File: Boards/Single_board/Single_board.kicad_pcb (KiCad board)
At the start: 2 copper layers, 170.1 x 185.4 mm, 116 parts, among them J1 Conn_01x04_Socket, J2 Conn_01x04_Socket, Q1 SI2306, Q10 SI2306, Q11 SI2306, Q12 SI2306, Q13 SI2306, Q14 SI2306, Q15 SI2306, Q2 SI2306, Q3 SI2306, Q4 SI2306, Q5 SI2306, Q6 SI2306, Q7 SI2306, Q8 SI2306, Q9 SI2306, SW1 +, SW10 5, SW11 2, SW12 9, SW13 PRO, SW14 6, SW15 3, SW16 CLR, SW17 ENTR, SW18 RSET, SW19 KEYREL, SW2 VERB, SW3 NOUN, SW4 0, SW5 7, SW6 -, SW7 4, SW8 1, SW9 8, U1 PCF8575

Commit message: some progress on the arduino boilerplate
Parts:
- removed A1: Arduino_Nano_Socket, PCM_arduino-library:Arduino_Nano_Socket
- added C3: 100nF, Capacitor_SMD:C_0805_2012Metric, F.Cu at (141.6, 146.4)
- added C4: 4.7uF, Capacitor_SMD:C_0805_2012Metric, F.Cu at (141.6, 152.2)
- added C5: 100nF, Capacitor_SMD:C_0805_2012Metric, F.Cu at (158.0, 151.2)
- added J3: USB_C_Receptacle_USB2.0_16P, Connector_USB:USB_C_Receptacle_G-Switch_GT-USB-7010ASV, F.Cu at (189.7, 149.3)
- added U2: ATmega328P-A, Package_QFP:TQFP-32_7x7mm_P0.8mm, F.Cu at (150.4, 149.8)
- added U3: CH340G, Package_SO:SOIC-16_3.9x9.9mm_P1.27mm, F.Cu at (172.0, 149.0)
- C1, C2: footprint Capacitor_SMD:C_1206_3216Metric_Pad1.33x1.80mm_HandSolder -> Capacitor_SMD:C_0805_2012Metric
- D20, D21, D22, D23, D24, D25, D26, D27, D28, D29, D30, D31, D32, D33: footprint LED_SMD:LED_1206_3216Metric_Pad1.42x1.75mm_HandSolder -> LED_SMD:LED_1206_3216Metric
- Q1, Q10, Q11, Q12, Q13, Q14, Q15, Q2, Q3, Q4, Q5, Q6, Q7, Q8, Q9: footprint Package_TO_SOT_SMD:SOT-23-3 -> Package_TO_SOT_SMD:SOT-23
- R1, R2, R3: footprint Resistor_SMD:R_1206_3216Metric_Pad1.30x1.75mm_HandSolder -> Resistor_SMD:R_1206_3216Metric
- R10, R11, R12, R13, R14, R15, R16, R17, R18, R19, R20, R21, R22, R23, R24, R25, R26, R27, R9: moved to F.Cu
- moved R26 143.3 mm to (143.3, 179.1)
- moved R27 143.3 mm to (143.3, 203.7)
- moved R10 133.4 mm to (272.1, 203.7)
- moved R9 133.1 mm to (272.0, 179.2)
- moved R36 117.8 mm to (138.5, 139.3)
- moved R35 111.6 mm to (138.4, 124.3)
- moved R34 106.2 mm to (138.5, 109.2)
- moved R11 103.2 mm to (266.5, 166.7)
- moved R12 103.2 mm to (266.5, 191.4)
- moved R13 103.2 mm to (266.5, 216.0)
- moved R24 94.3 mm to (167.8, 191.5)
- moved R25 94.3 mm to (167.8, 216.1)
- moved R23 94.0 mm to (167.9, 166.7)
- moved R29 93.7 mm to (138.3, 48.9)
- moved R3 93.0 mm to (161.4, 100.8), turned to 90 degrees
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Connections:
- U1 pad 10: No Att -> No Dap
- U1 pad 11: Uplink -> Prio Disp
- U1 pad 13: Temp -> Vel
- U1 pad 14: Gimbal Lock -> Alt
- U1 pad 15: Prog -> Tracker
- U1 pad 17: Tracker -> Prog
- U1 pad 18: Alt -> Gimbal Lock
- U1 pad 19: Vel -> Temp
- U1 pad 5: Prio Disp -> Uplink
- U1 pad 6: No Dap -> No Att
- U1 pad 7: Opr Err -> STBY
- U1 pad 9: STBY -> Opr Err
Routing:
- removed copper zone on B.Cu, net GND
- removed copper zone on B.Cu, net PWMcom
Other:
- board size 170.1 x 185.4 mm -> 169.9 x 190.9 mm
- board text added: "ASPlab [DSKY] Unified Board Rev. 0.5.x"
- board text added: "Rev. 0.5.x"
- board text removed: "ASPlab [DSKY] Main Board Rev. 0.4.x"
- board text removed: "DSKY Crew Prototyping board, Alarm Board Rev. 0.4.x"

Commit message: Single board nearly ready to order
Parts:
- added C6: 4.7uF, Capacitor_SMD:C_0805_2012Metric, F.Cu at (165.4, 149.0)
- added C7: 100nF, Capacitor_SMD:C_0805_2012Metric, F.Cu at (163.4, 149.0)
- added C8: 100nF, Capacitor_SMD:C_0805_2012Metric, F.Cu at (170.3, 143.6)
- added C9: 100nF, Capacitor_SMD:C_0805_2012Metric, F.Cu at (170.4, 154.4)
- added D34: SD101AWS, Diode_SMD:D_SOD-323, F.Cu at (181.4, 143.2)
- added J4: ICSP, Connector_PinHeader_2.54mm:PinHeader_2x03_P2.54mm_Vertical_SMD, F.Cu at (171.4, 135.2)
- added R44: 5.1k, Resistor_SMD:R_0603_1608Metric, F.Cu at (184.0, 151.6)
- added R45: 5.1k, Resistor_SMD:R_0603_1608Metric, F.Cu at (182.4, 151.6)
- added R46: 1k, Resistor_SMD:R_0603_1608Metric, F.Cu at (160.0, 144.6)
- added R47: 1k, Resistor_SMD:R_0603_1608Metric, F.Cu at (160.0, 142.8)
- added R48: 0, Jumper:SolderJumper-2_P1.3mm_Open_RoundedPad1.0x1.5mm, F.Cu at (161.4, 88.8)
- J1: value Conn_01x04_Socket -> AUX_I2C_1
- J2: value Conn_01x04_Socket -> AUX_I2C_2
- U3: value CH340G -> CH340C
- moved Q1 0.50 mm to (165.0, 89.4)
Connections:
- J3 pad A1: Net-(J3-GND-PadA1) -> GND
- J3 pad A12: Net-(J3-GND-PadA1) -> GND
- J3 pad A5: unconnected-(J3-CC1-PadA5) -> Net-(J3-CC1)
- J3 pad A6: unconnected-(J3-D+-PadA6) -> Net-(U3-UD+)
- J3 pad A7: unconnected-(J3-D--PadA7) -> Net-(U3-UD-)
- J3 pad B1: Net-(J3-GND-PadA1) -> GND
- J3 pad B12: Net-(J3-GND-PadA1) -> GND
- J3 pad B5: unconnected-(J3-CC2-PadB5) -> Net-(J3-CC2)
- J3 pad B6: unconnected-(J3-D+-PadB6) -> Net-(U3-UD+)
- J3 pad B7: unconnected-(J3-D--PadB7) -> Net-(U3-UD-)
- J3 pad S1: unconnected-(J3-SHIELD-PadS1) -> GND
- Q1 pad 3: PWMcom -> Net-(Q1-D)
- R2 pad 1: PWMcom -> Net-(Q1-D)
- U2 pad 29: 328P_RESET -> RESET
- U2 pad 30: unconnected-(U2-PD0-Pad30) -> UC_RX
- U2 pad 31: unconnected-(U2-PD1-Pad31) -> UC_TX
- U3 pad 1: unconnected-(U3-GND-Pad1) -> GND
- U3 pad 13: unconnected-(U3-~{DTR}-Pad13) -> Net-(U3-~{DTR})
- U3 pad 16: unconnected-(U3-VCC-Pad16) -> +5V
- U3 pad 2: unconnected-(U3-TXD-Pad2) -> Net-(U3-TXD)
- U3 pad 3: unconnected-(U3-RXD-Pad3) -> Net-(U3-RXD)
- U3 pad 4: unconnected-(U3-V3-Pad4) -> Net-(U3-V3)
- U3 pad 5: unconnected-(U3-UD+-Pad5) -> Net-(U3-UD+)
- U3 pad 6: unconnected-(U3-UD--Pad6) -> Net-(U3-UD-)
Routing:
- net +5V: track 0.00 -> 888.7 mm
- net PWMcom: track 0.00 -> 866.8 mm, vias 0 -> 1
- net GND: track 0.00 -> 290.0 mm, vias 0 -> 1
- net SDA: track 0.00 -> 247.1 mm, vias 0 -> 2
- net X4: track 0.00 -> 215.6 mm, vias 0 -> 1
- net Y1: track 0.00 -> 208.8 mm, vias 0 -> 3
- net Y2: track 0.00 -> 195.4 mm, vias 0 -> 1
- net X3: track 0.00 -> 189.9 mm, vias 0 -> 2
- net Y3: track 0.00 -> 170.1 mm
- net Net-(D2-A): track 0.00 -> 157.3 mm, vias 0 -> 1
- net Net-(D19-A): track 0.00 -> 153.6 mm
- net Net-(D1-A): track 0.00 -> 142.5 mm, vias 0 -> 1
- net SCL: track 0.00 -> 139.2 mm, vias 0 -> 3
- net Net-(D18-A): track 0.00 -> 138.4 mm, vias 0 -> 1
- net X2: track 0.00 -> 117.9 mm, vias 0 -> 1
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- added copper zone on B.Cu, net GND
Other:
- outline, holes or cut-outs redrawn

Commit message: Fixes on single board
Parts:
- D34: value SD101AWS -> MBR0520LT1G; footprint Diode_SMD:D_SOD-323 -> Diode_SMD:D_SOD-123
- SW1, SW10, SW11, SW12, SW13, SW14, SW15, SW16, SW17, SW18, SW19, SW2, SW3, SW4, SW5, SW6, SW7, SW8, SW9: footprint Button_Switch_Keyboard:SW_Cherry_MX_1.00u_PCB -> Switch_Misc:SW_Cherry_MX_1.00u_PCB
- moved R33 63.7 mm to (169.4, 124.9), turned to 0 degrees
- moved R28 63.7 mm to (160.5, 124.8), turned to 180 degrees
- moved J3 2.64 mm to (192.4, 149.2)
- moved R44 2.64 mm to (186.6, 151.5)
- moved R45 2.64 mm to (185.0, 151.5)
- moved D34 2.01 mm to (183.4, 143.1)
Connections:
- R28 pad 1: SCK -> SCL
- U1 pad 22: SCK -> SCL
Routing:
- net SCL: track 139.2 -> 241.6 mm
- net SCK: track 103.0 -> 26.2 mm, vias 3 -> 2
- net PWMcom: track 866.8 -> 846.2 mm
- net Net-(D34-A): track 35.8 -> 16.4 mm
- net SDA: track 247.1 -> 232.1 mm, vias 2 -> 3
- net Net-(D29-A): track 12.4 -> 23.3 mm
- net Net-(D16-A): track 99.7 -> 90.4 mm
- net X3: track 189.9 -> 180.7 mm, vias 2 -> 1
- net +5V: track 888.7 -> 896.6 mm
- net Net-(U3-RXD): track 15.2 -> 22.9 mm
- net Net-(D2-A): track 157.3 -> 149.7 mm
- net Uplink: track 41.6 -> 49.1 mm
- net No Dap: track 51.2 -> 58.3 mm
- net Opr Err: track 37.3 -> 44.4 mm
- net Net-(U3-UD+): track 16.4 -> 22.2 mm, vias 0 -> 2
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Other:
- outline, holes or cut-outs redrawn

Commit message: Visual Schematic improvements
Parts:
- SW1, SW10, SW11, SW12, SW13, SW14, SW15, SW16, SW17, SW18, SW19, SW2, SW3, SW4, SW5, SW6, SW7, SW8, SW9: footprint Switch_Misc:SW_Cherry_MX_1.00u_PCB -> Button_Switch_Keyboard:SW_Cherry_MX_1.00u_PCB
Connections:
- net PWMcom renamed PWMCom

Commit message: fix cherry 3d models in footprints
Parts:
- SW1, SW10, SW11, SW12, SW13, SW14, SW15, SW16, SW17, SW18, SW19, SW2, SW3, SW4, SW5, SW6, SW7, SW8, SW9: footprint Button_Switch_Keyboard:SW_Cherry_MX_1.00u_PCB -> Switch_Misc:SW_Cherry_MX_1.00u_PCB

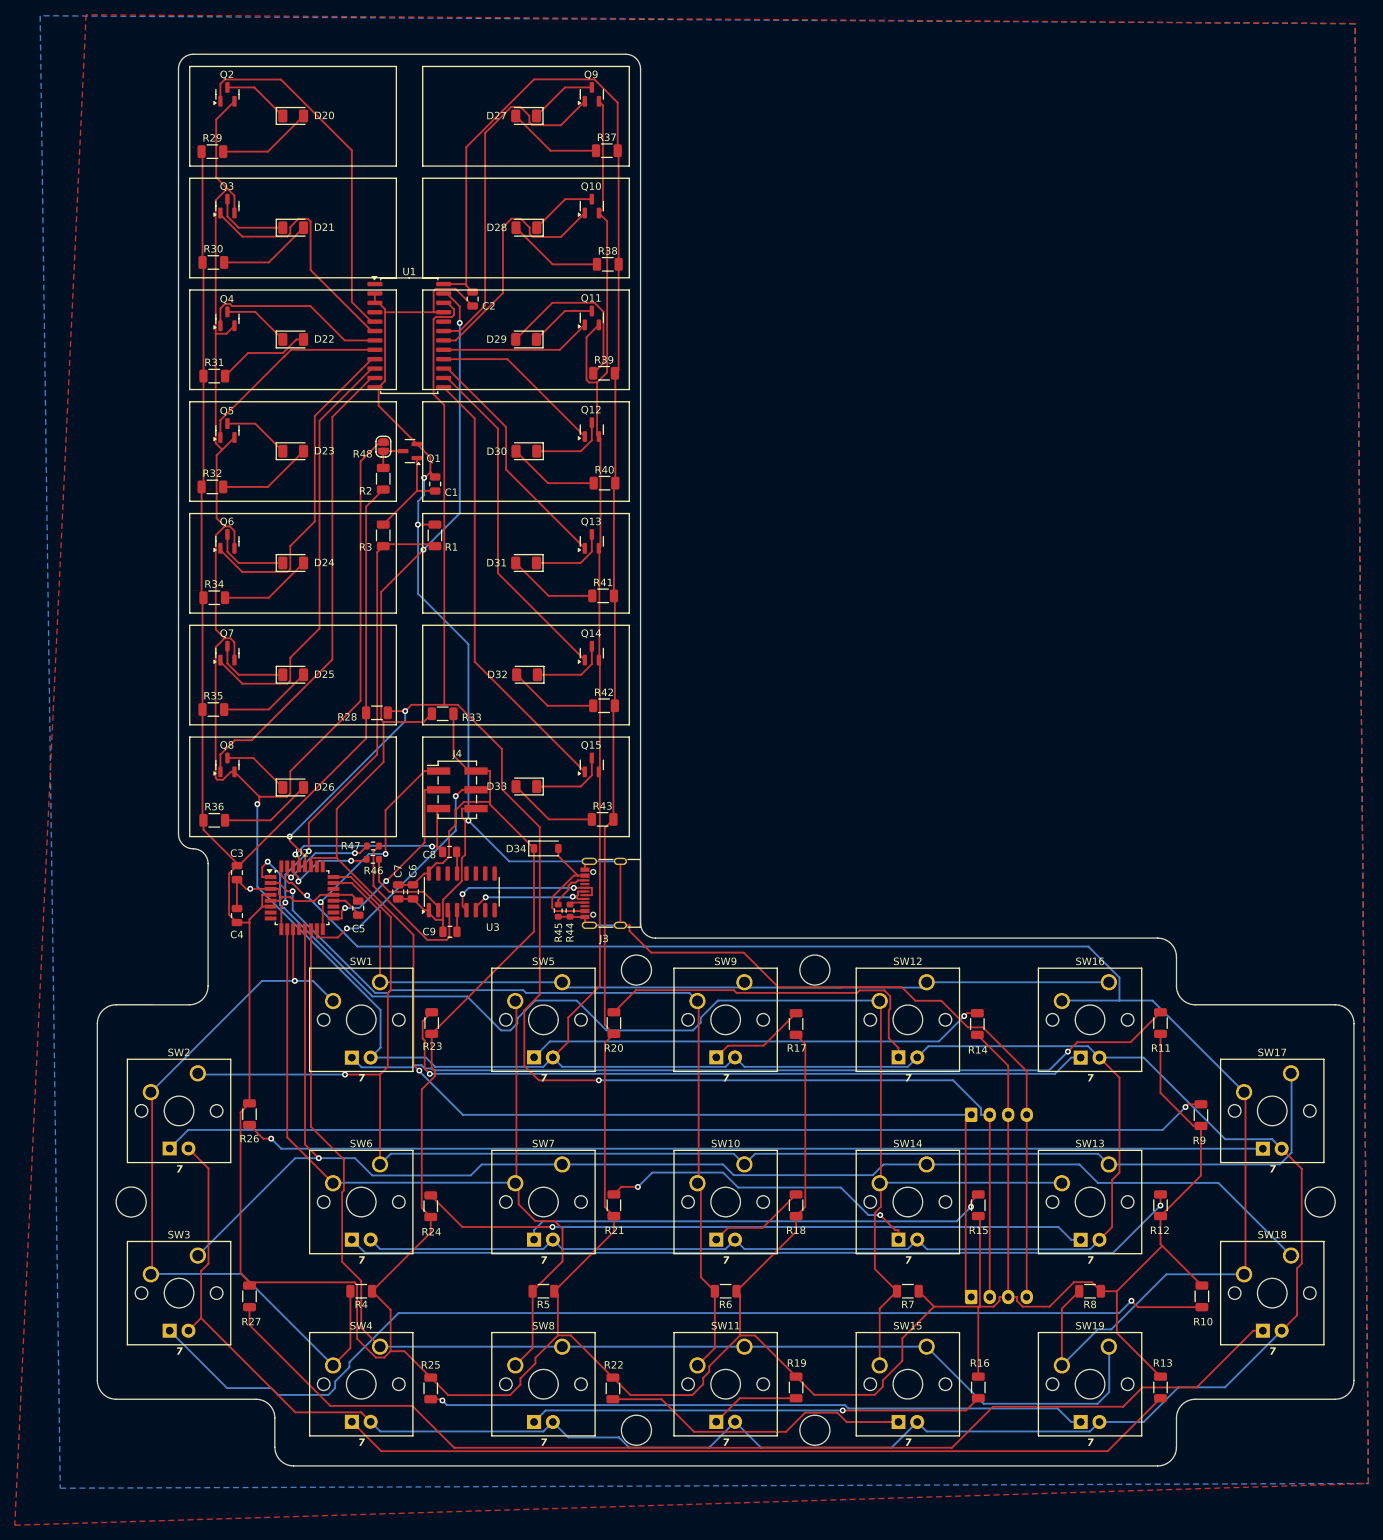
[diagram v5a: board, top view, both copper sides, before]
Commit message: Re-stitch and clean up redundant tracks.  Correct some port directions.
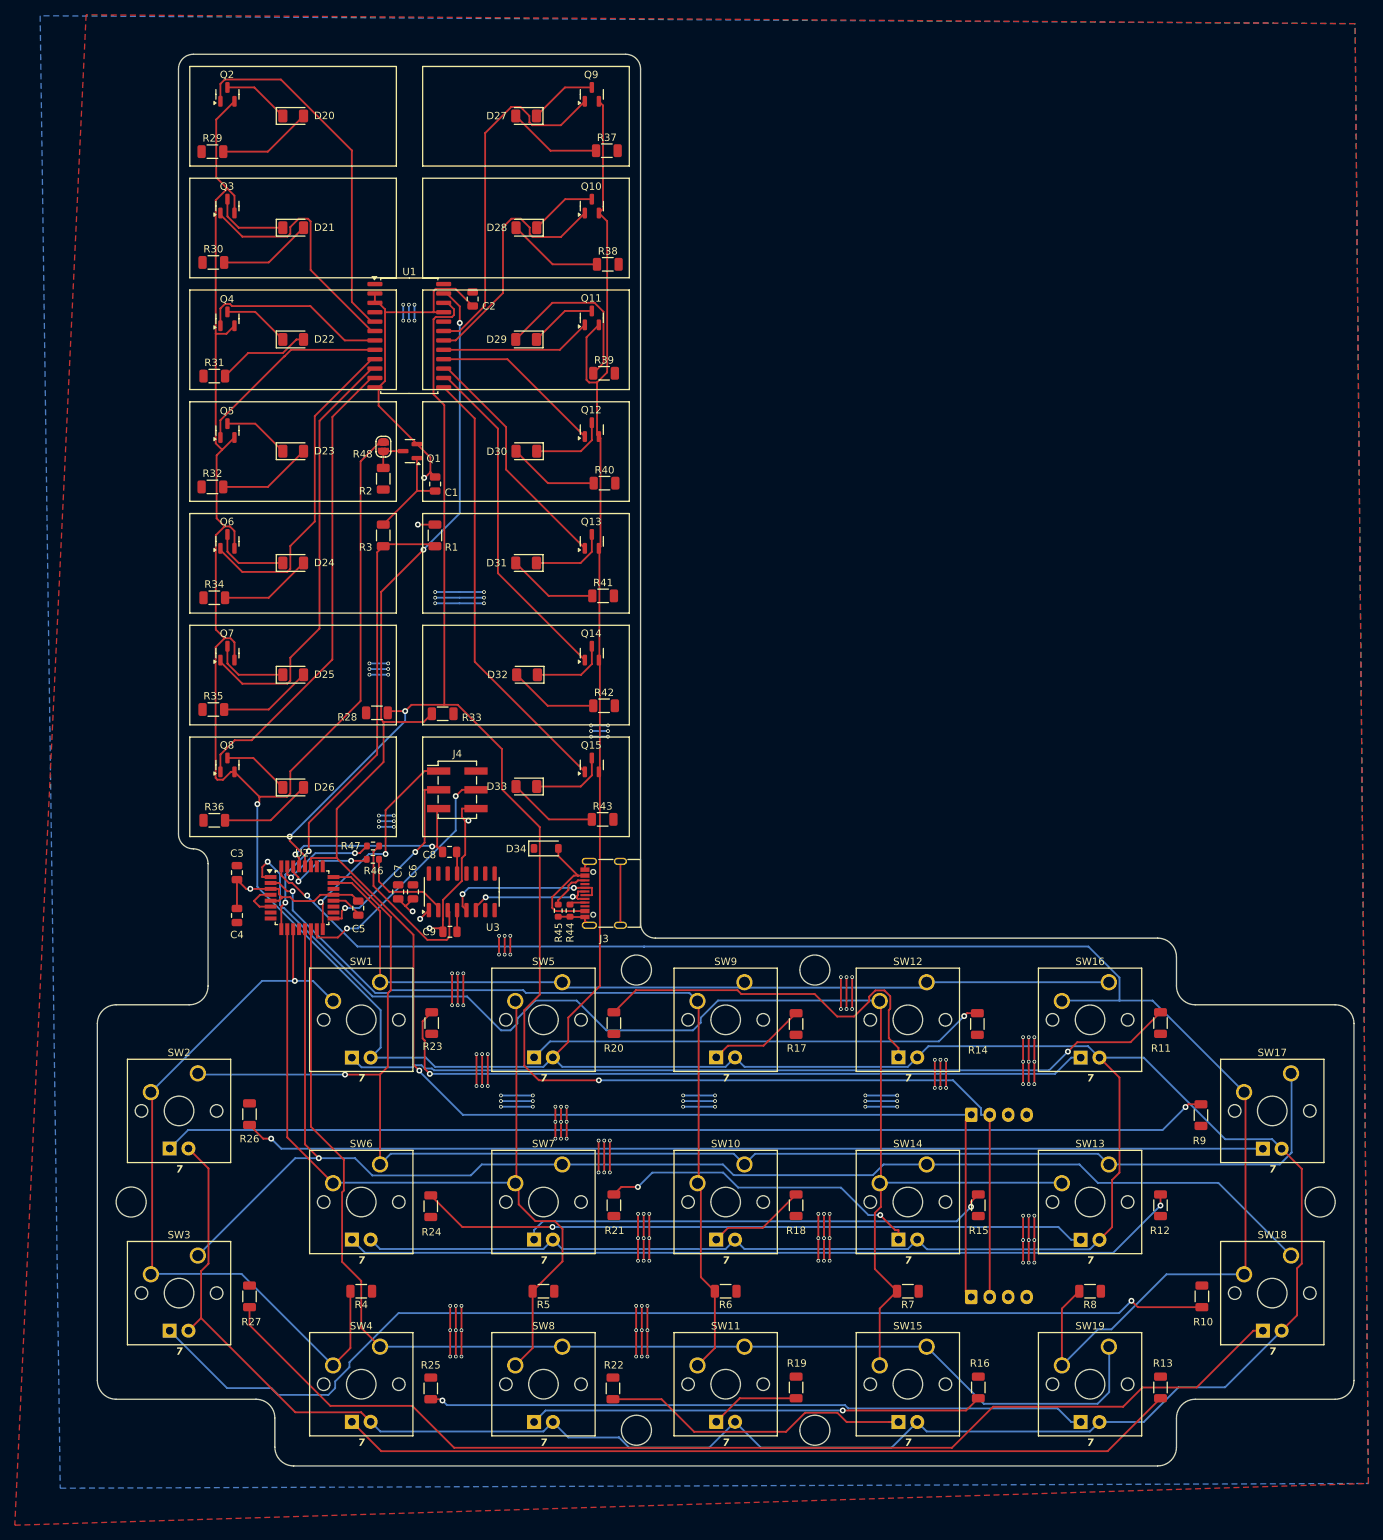
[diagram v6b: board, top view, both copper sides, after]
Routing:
- net +5V: track 896.6 -> 90.9 mm, vias 0 -> 48
- net GND: track 288.4 -> 319.8 mm, vias 4 -> 106
- net Net-(D12-A): track 48.1 -> 51.1 mm

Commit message: Remove redundant GND tracks in place of vias.  Continue rerouting & condensing.  Make PWMCom 20mil
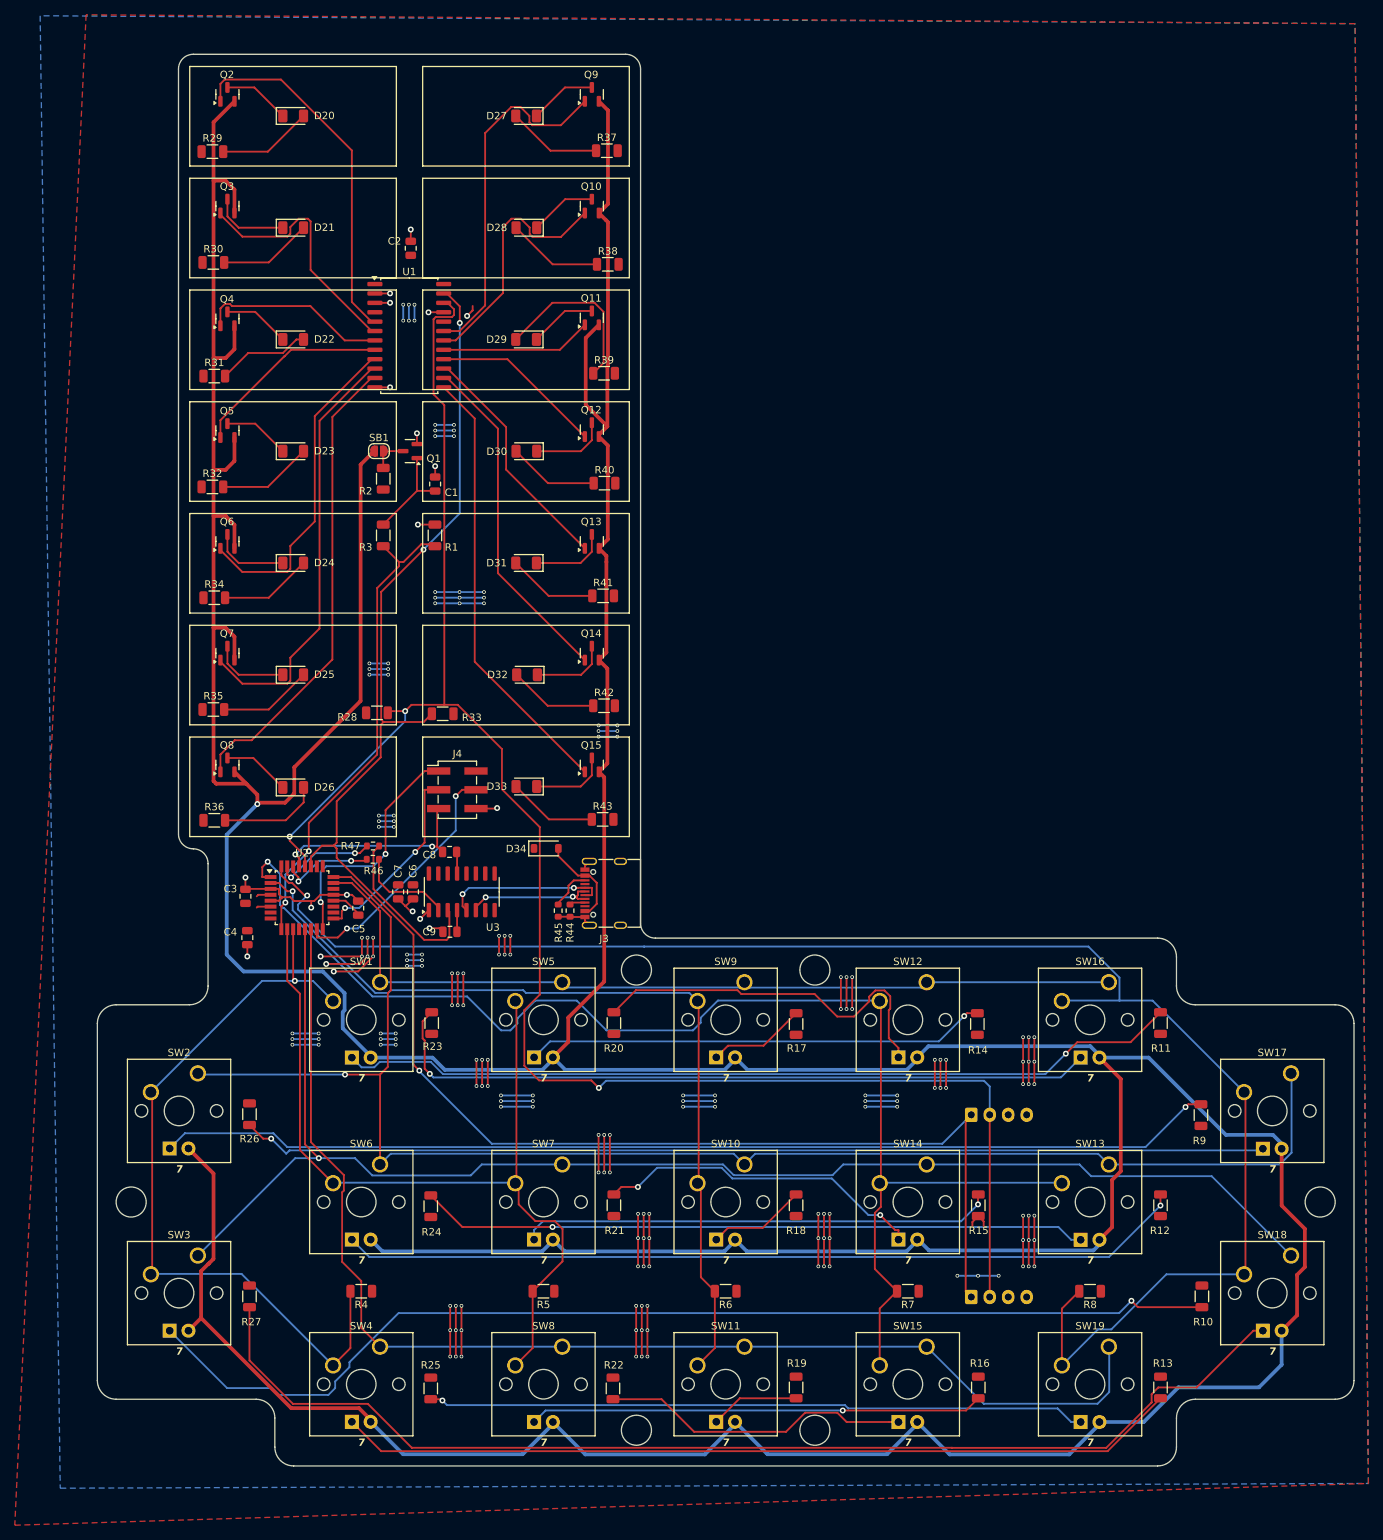
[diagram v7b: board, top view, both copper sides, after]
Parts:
- removed R48: 0, Jumper:SolderJumper-2_P1.3mm_Open_RoundedPad1.0x1.5mm
- added SB1: 0, Jumper:SolderJumper-2_P1.3mm_Open_RoundedPad1.0x1.5mm, F.Cu at (160.8, 89.4)
- moved C2 10.8 mm to (165.1, 62.0), turned to 90 degrees
- moved C3 3.41 mm to (142.7, 149.6), turned to 90 degrees
- moved C4 3.31 mm to (143.0, 155.2), turned to -90 degrees
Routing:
- net PWMCom: track 846.2 -> 890.2 mm
- net GND: track 319.8 -> 278.3 mm, vias 106 -> 116
- net +5V: track 90.9 -> 130.0 mm, vias 48 -> 78
- net SDA: track 232.1 -> 236.0 mm
- net Net-(D34-A): track 16.4 -> 12.6 mm
- net Net-(D19-A): track 152.9 -> 156.4 mm
- net X4: track 218.8 -> 221.6 mm
- net SCL: track 241.6 -> 244.1 mm
- net MISO: track 30.5 -> 33.0 mm
- net Net-(D1-A): track 141.9 -> 143.5 mm
- net Net-(D26-A): track 12.4 -> 13.7 mm
- net Net-(D3-A): track 113.5 -> 114.3 mm
- net Net-(D18-A): track 138.4 -> 138.9 mm
- net Net-(D13-A): track 44.2 -> 44.7 mm
- net PWM: track 64.7 -> 65.2 mm
